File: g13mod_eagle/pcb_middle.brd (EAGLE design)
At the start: 134.2 x 33.2 mm, 0 parts

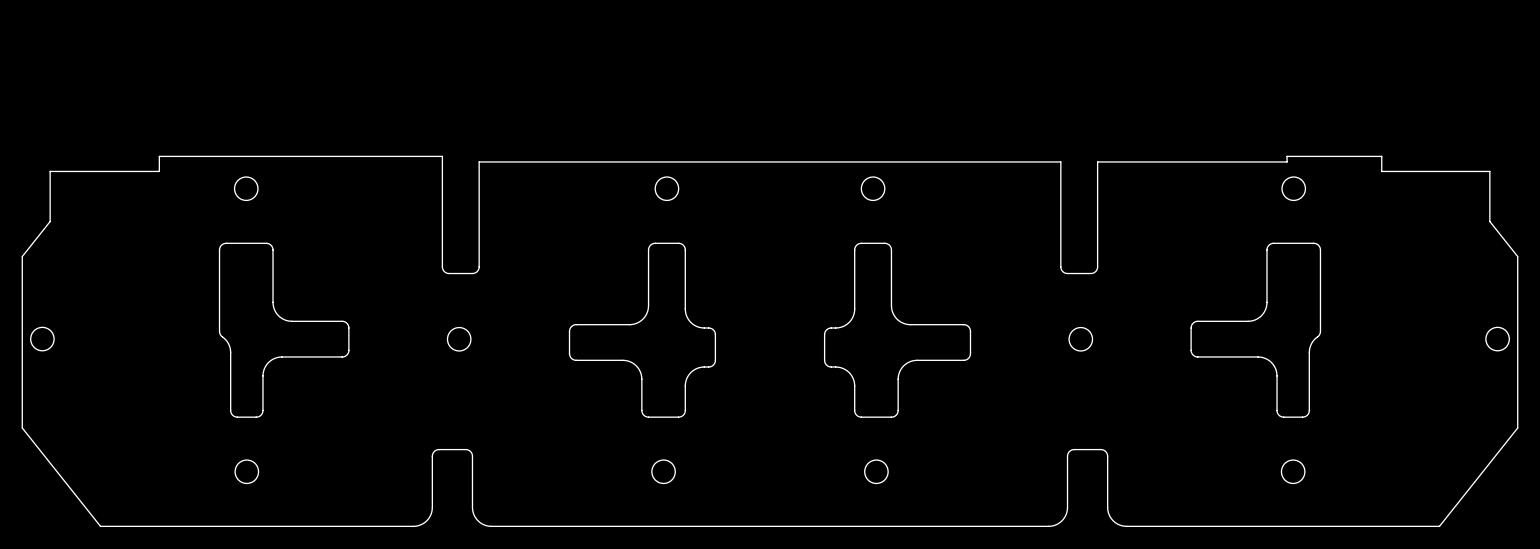
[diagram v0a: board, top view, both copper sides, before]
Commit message: Add switches
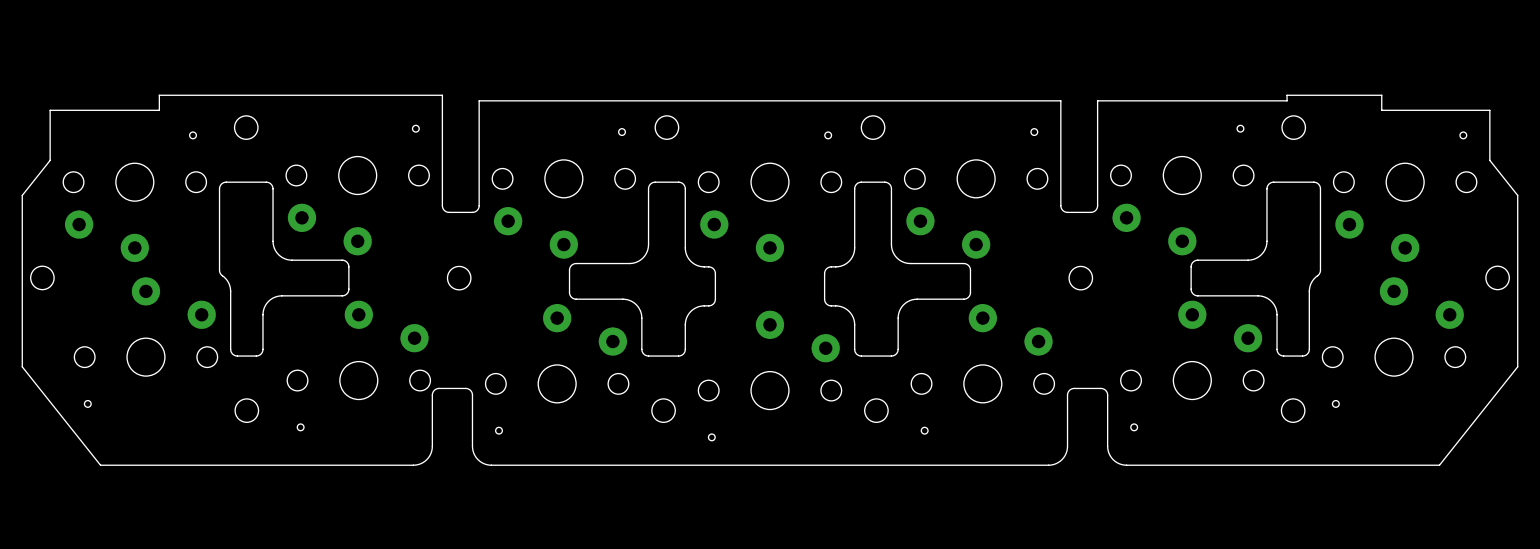
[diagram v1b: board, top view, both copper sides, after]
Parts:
- added U$1, U$10, U$11, U$12, U$13, U$14, U$2, U$3, U$4, U$5, U$6, U$7, U$8, U$9: KEYSWITCH-PLAIN-CHOC-1U, Keyboard:CHOC-1U
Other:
- outline, holes or cut-outs redrawn

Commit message: wiring middle pcb
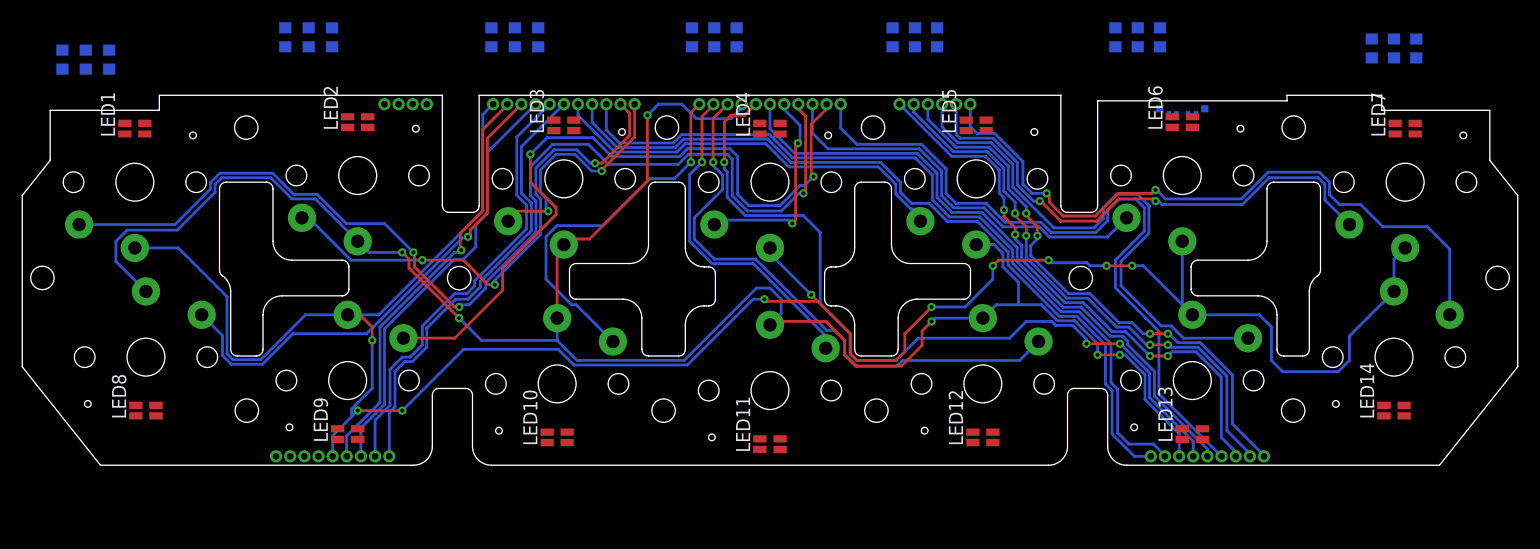
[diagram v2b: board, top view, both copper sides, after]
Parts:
- removed U$9: KEYSWITCH-PLAIN-CHOC-1U, Keyboard:CHOC-1U
- added D1: QLS6B-FKW-CNSNSF043, QLS6B-FKW-CNSNSF043:LED_QLS6B-FKW-CNSNSF043
- added G9: KEYSWITCH-PLAIN-CHOC-1U, Keyboard:CHOC-1U
- added JP1: (no value), pinhead-half-pitch:THROUHOLE04
- added JP2, JP3: (no value), pinhead-half-pitch:THROUHOLE11
- added JP4: (no value), pinhead-half-pitch:THROUHOLE06
- added JP8, JP9: (no value), pinhead-half-pitch:THROUHOLE09
- added LED1, LED10, LED11, LED12, LED13, LED14, LED2, LED3, LED4, LED5, LED6, LED7, LED8, LED9: B38G3RGB, led_rgb:B38G3RGB
- added R1, R10, R11, R12, R13, R14, R15, R16, R17, R18, R19, R2, R20, R21, R3, R4, R5, R6, R7, R8, R9: (no value), rcl:R0603
- renumbered U$1 to G1, U$10 to G10, U$11 to G11, U$12 to G12, U$13 to G13, U$14 to G14, U$2 to G2, U$3 to G6, U$4 to G3, U$5 to G5, U$6 to G4, U$7 to G7, U$8 to G8
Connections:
- new net B: JP1.4, JP8.9, R11.1, R14.1, R17.1, R2.1, R20.1, R5.1, R8.1
- new net CN6_10: G5.CHOC2, JP2.5
- new net CN6_11: JP2.6, JP8.1
- new net CN6_13: JP2.7, JP8.2
- new net CN6_14: JP2.8, JP8.3
- new net CN6_16: G8.CHOC2, JP2.9
- new net CN6_17: JP2.10, JP8.4
- new net CN6_18: G1.CHOC1, G13.CHOC1, G14.CHOC1, G4.CHOC1, G6.CHOC1, G7.CHOC1, G9.CHOC1, JP2.11, JP8.5
- new net CN6_3: G12.CHOC2, JP3.9
- new net CN6_4: G11.CHOC2, JP3.10
- new net CN6_5: G10.CHOC2, JP3.11
- new net CN6_6: G3.CHOC2, JP2.1
- new net CN6_7: G2.CHOC2, JP2.2
- new net CN6_8: JP2.3, JP9.8
- new net CN6_9: JP2.4, JP9.9
- new net CN7_1: G14.CHOC2, JP4.1
- new net CN7_10: G6.CHOC2, JP3.3
- new net CN7_11: G1.CHOC2, JP3.4
- new net CN7_12: G4.CHOC2, JP3.5
- new net CN7_13: JP3.6, JP9.5
- new net CN7_14: JP3.7, JP9.6
- new net CN7_15: G10.CHOC1, G11.CHOC1, G12.CHOC1, G2.CHOC1, G3.CHOC1, G5.CHOC1, G8.CHOC1, JP3.8, JP9.7
- new net CN7_2: G7.CHOC2, JP4.2
- new net CN7_3: G13.CHOC2, JP4.3
- new net CN7_4: JP4.4, JP9.1
- new net CN7_6: JP4.5, JP9.2
- new net CN7_7: JP4.6, JP9.3
- new net CN7_8: JP3.1, JP9.4
- new net CN7_9: G9.CHOC2, JP3.2
- new net G: JP1.2, JP8.7, R1.1, R10.1, R13.1, R16.1, R19.1, R4.1, R7.1
- new net N$1: LED1.1, R1.2
- new net N$10: LED4.1, R10.2
- new net N$11: LED4.2, R11.2
- new net N$12: LED4.4, R12.2
- new net N$13: LED5.1, R13.2
- new net N$14: LED5.2, R14.2
- new net N$15: LED5.4, R15.2
- new net N$16: LED6.1, R16.2
- new net N$17: LED6.2, R17.2
- new net N$18: LED6.4, R18.2
- new net N$19: LED7.1, R19.2
- new net N$2: LED1.2, R2.2
- new net N$20: LED7.2, R20.2
- new net N$21: LED7.4, R21.2
- new net N$3: LED1.4, R3.2
- new net N$4: LED2.1, R4.2
- new net N$5: LED2.2, R5.2
- new net N$6: LED2.4, R6.2
- new net N$7: LED3.1, R7.2
- new net N$8: LED3.2, R8.2
- new net N$9: LED3.4, R9.2
- new net R: JP1.3, JP8.8, R12.1, R15.1, R18.1, R21.1, R3.1, R6.1, R9.1
- new net V: D1.1, D1.3, D1.5, JP1.1, JP8.6, LED1.3, LED10.3, LED11.3, LED12.3, LED13.3, LED14.3, LED2.3, LED3.3, LED4.3, LED5.3, LED6.3, LED7.3, LED8.3, LED9.3
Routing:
- net CN6_18: track 0.00 -> 206.6 mm, vias 0 -> 10
- net CN7_15: track 0.00 -> 175.7 mm, vias 0 -> 6
- net CN7_11: track 0.00 -> 97.6 mm, vias 0 -> 3
- net CN7_14: track 0.00 -> 71.9 mm, vias 0 -> 3
- net CN6_8: track 0.00 -> 71.6 mm
- net CN6_9: track 0.00 -> 70.4 mm
- net CN7_9: track 0.00 -> 65.2 mm, vias 0 -> 2
- net CN7_8: track 0.00 -> 64.0 mm
- net CN7_1: track 0.00 -> 61.6 mm, vias 0 -> 2
- net CN7_13: track 0.00 -> 57.5 mm
- net CN6_3: track 0.00 -> 51.3 mm, vias 0 -> 1
- net CN7_4: track 0.00 -> 50.7 mm, vias 0 -> 4
- net CN7_7: track 0.00 -> 50.5 mm, vias 0 -> 4
- net CN7_6: track 0.00 -> 50.2 mm, vias 0 -> 4
- net CN7_3: track 0.00 -> 49.5 mm
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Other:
- outline, holes or cut-outs redrawn

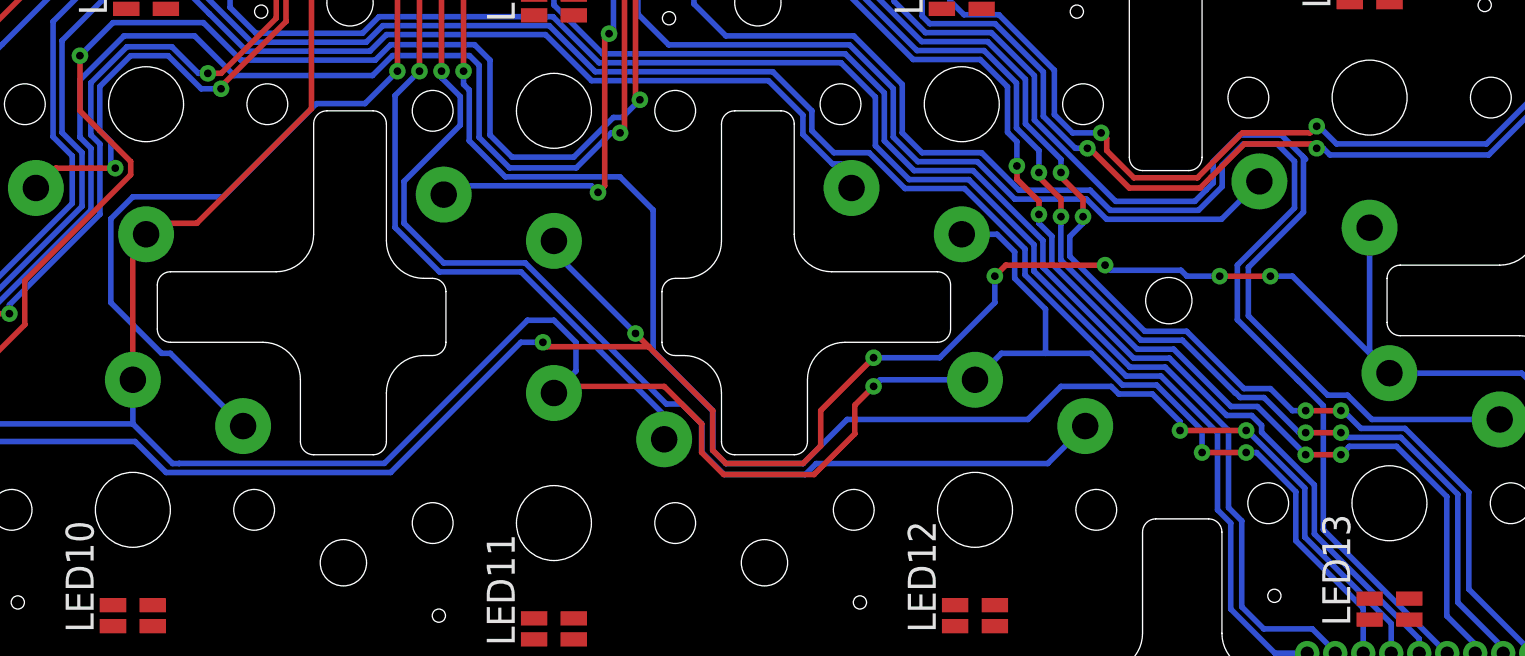
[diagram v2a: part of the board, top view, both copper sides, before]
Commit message: wiring middle pcb
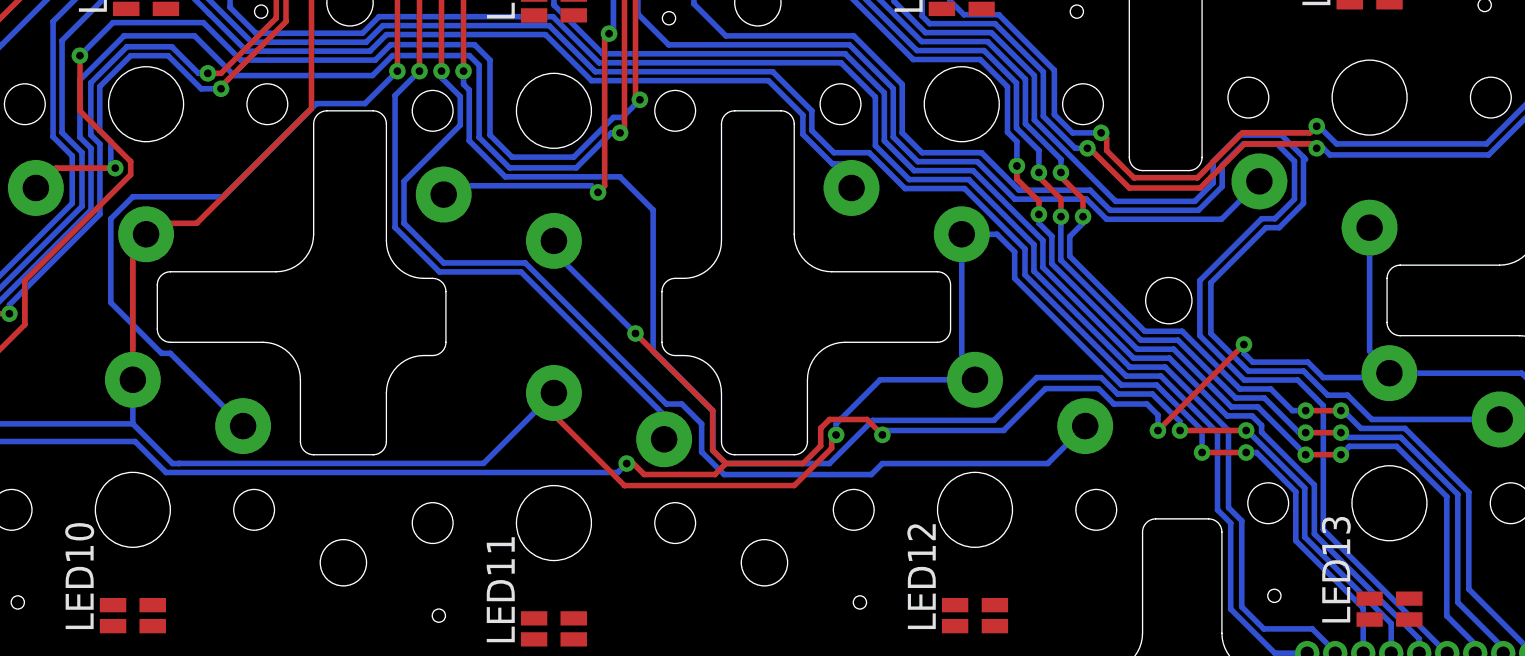
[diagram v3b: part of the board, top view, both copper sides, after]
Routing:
- net CN7_15: track 175.7 -> 171.3 mm
- net CN7_3: track 49.5 -> 52.7 mm
- net CN7_8: track 64.0 -> 67.2 mm
- net CN6_18: track 206.6 -> 206.9 mm, vias 10 -> 8

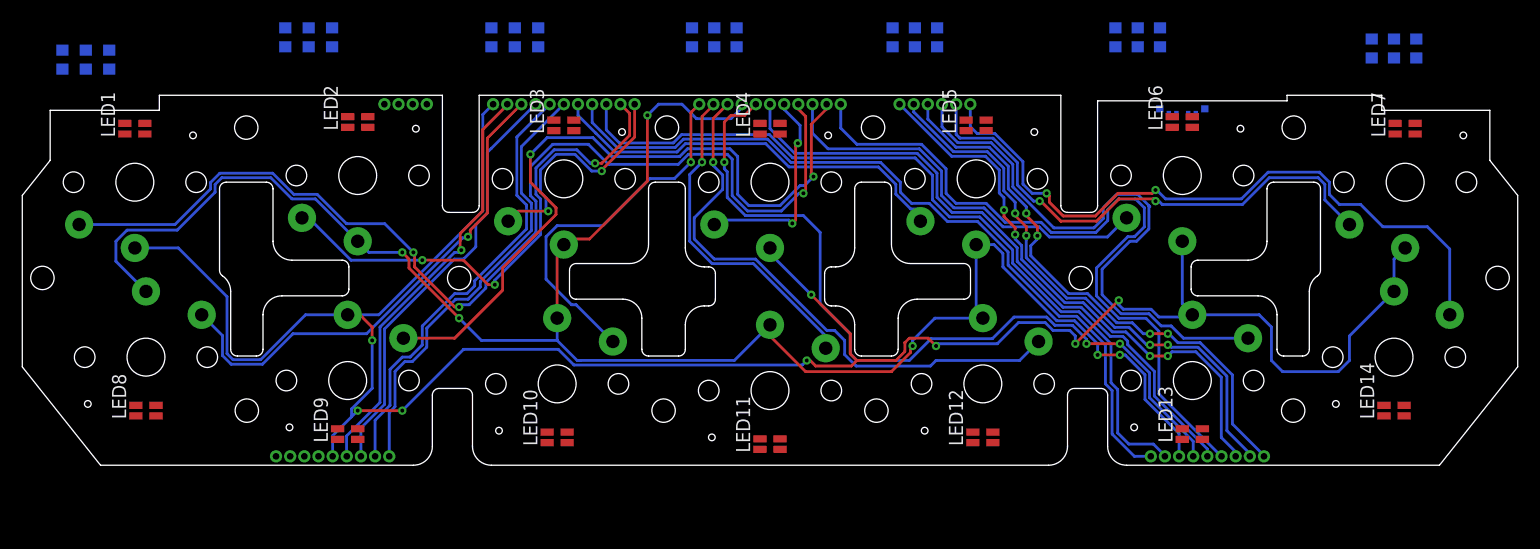
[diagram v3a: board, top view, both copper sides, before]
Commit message: wiring middle pcb
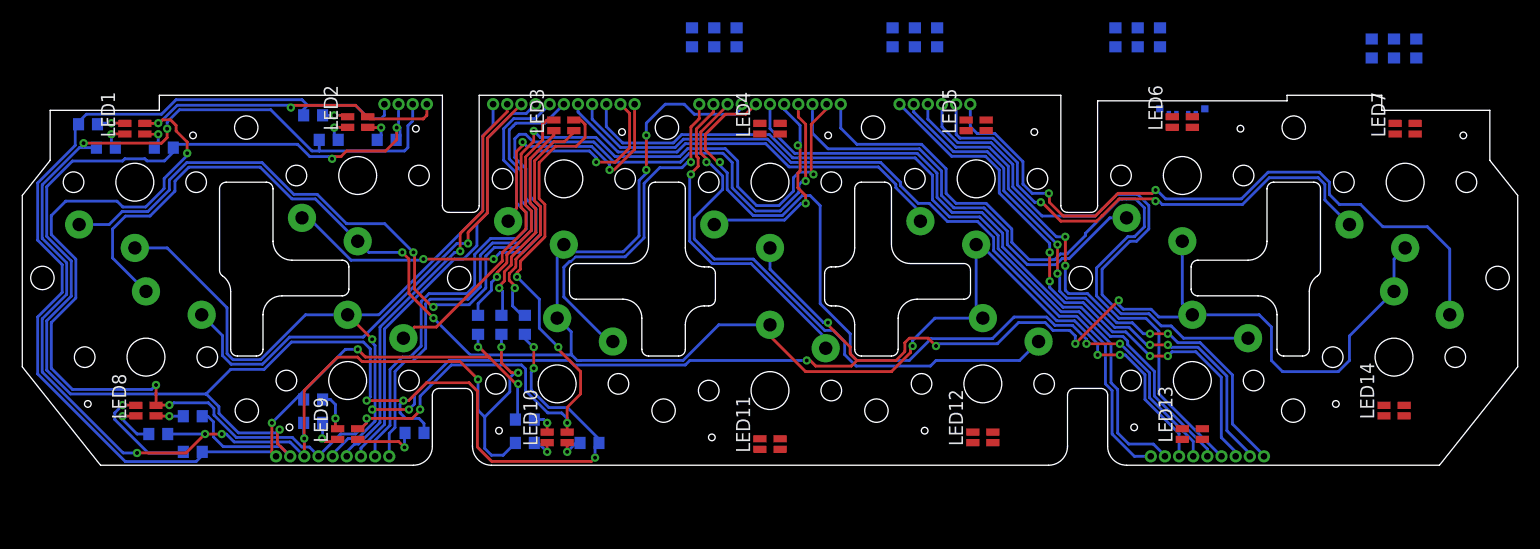
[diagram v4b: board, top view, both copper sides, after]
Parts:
- added R22, R23, R24, R25, R26, R27, R28, R29, R30: (no value), rcl:R0603
- moved R8 26.4 mm to (-26.2, -12.8)
- moved R9 26.0 mm to (-22.0, -12.8)
- moved R7 25.8 mm to (-24.1, -12.8)
- moved R6 12.9 mm to (-34.4, 3.80), turned to 0 degrees
- moved R3 12.1 mm to (-54.4, 3.10), turned to 0 degrees
- moved R4 9.37 mm to (-39.6, 3.80), turned to 180 degrees
- moved R1 8.10 mm to (-59.6, 3.10), turned to 180 degrees
- moved R5 7.20 mm to (-41.0, 6.00), turned to 180 degrees
- moved R2 6.10 mm to (-61.2, 5.20), turned to 180 degrees
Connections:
- new net N$22: LED8.1, R22.2
- new net N$23: LED8.2, R23.2
- new net N$24: LED8.4, R24.2
- new net N$25: LED9.1, R25.2
- new net N$26: LED9.2, R26.2
- new net N$27: LED9.4, R27.2
- new net N$28: LED10.1, R28.2
- new net N$29: LED10.2, R29.2
- new net N$30: LED10.4, R30.2
- net B: now also R23.1, R26.1, R29.1
- net G: now also R22.1, R25.1, R28.1
- net R: now also R24.1, R27.1, R30.1
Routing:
- net R: track 0.00 -> 163.5 mm, vias 0 -> 8
- net V: track 0.00 -> 160.3 mm, vias 0 -> 10
- net G: track 0.00 -> 139.8 mm, vias 0 -> 9
- net B: track 0.00 -> 118.7 mm, vias 0 -> 4
- net N$8: track 0.00 -> 21.1 mm, vias 0 -> 1
- net N$9: track 0.00 -> 21.0 mm, vias 0 -> 1
- net N$7: track 0.00 -> 19.2 mm, vias 0 -> 1
- net N$23: track 0.00 -> 10.2 mm, vias 0 -> 1
- net CN7_11: track 97.6 -> 104.5 mm
- net CN7_15: track 171.3 -> 178.1 mm, vias 6 -> 7
- net N$27: track 0.00 -> 6.17 mm, vias 0 -> 1
- net CN6_11: track 39.9 -> 45.1 mm
- net CN6_13: track 39.9 -> 44.7 mm
- net N$22: track 0.00 -> 4.40 mm, vias 0 -> 1
- net CN7_14: track 72.2 -> 76.5 mm
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
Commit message: wiring middle pcb
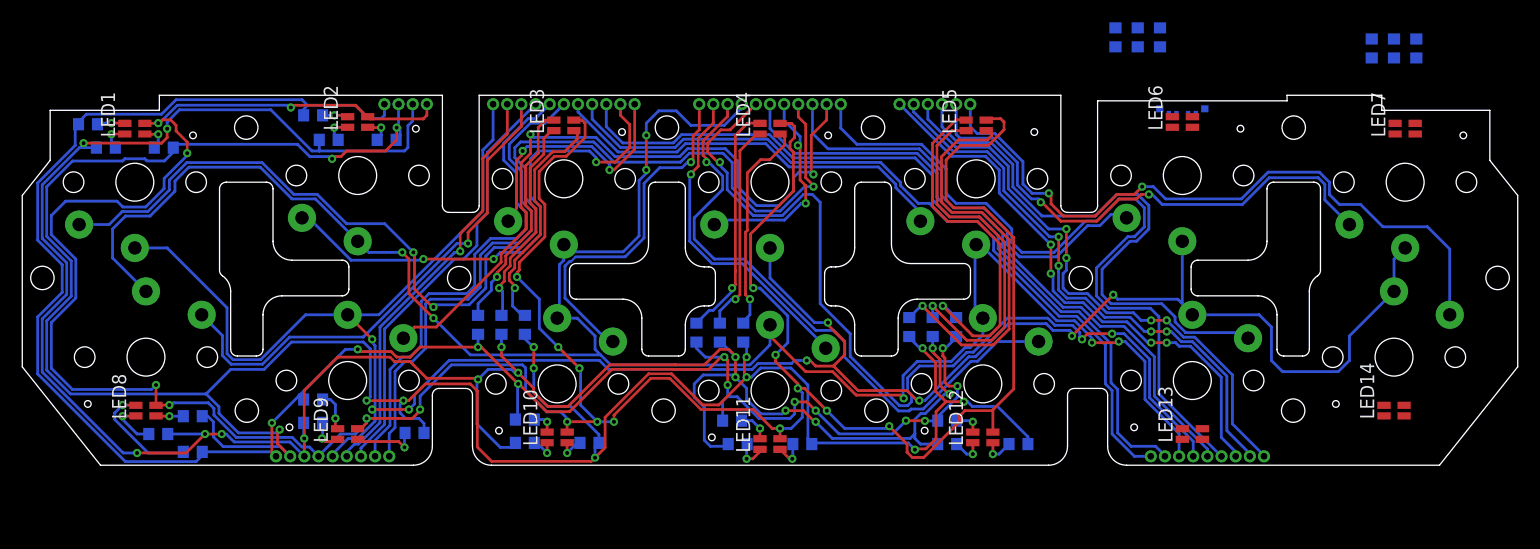
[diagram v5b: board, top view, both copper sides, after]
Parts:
- added R31, R32, R33, R34, R35, R36: (no value), rcl:R0603
- moved R12 26.9 mm to (-2.40, -13.5)
- moved R11 26.7 mm to (-6.60, -13.5)
- moved R10 26.5 mm to (-4.50, -13.5)
- moved R14 26.1 mm to (16.7, -13.0)
- moved R13 26.0 mm to (14.6, -13.0)
- moved R15 26.0 mm to (12.5, -13.0)
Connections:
- new net N$31: LED11.1, R31.2
- new net N$32: LED11.2, R32.2
- new net N$33: LED11.4, R33.2
- new net N$34: LED12.1, R34.2
- new net N$35: LED12.2, R35.2
- new net N$36: LED12.4, R36.2
- net B: now also R32.1, R35.1
- net G: now also R31.1, R34.1
- net R: now also R33.1, R36.1
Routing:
- net V: track 160.3 -> 279.6 mm, vias 10 -> 19
- net G: track 139.8 -> 209.2 mm, vias 9 -> 15
- net R: track 163.5 -> 231.6 mm, vias 8 -> 13
- net B: track 118.7 -> 181.8 mm, vias 4 -> 12
- net N$15: track 0.00 -> 37.0 mm, vias 0 -> 1
- net N$13: track 0.00 -> 32.8 mm, vias 0 -> 1
- net N$14: track 0.00 -> 32.6 mm, vias 0 -> 1
- net N$11: track 0.00 -> 21.2 mm, vias 0 -> 1
- net N$12: track 0.00 -> 19.7 mm, vias 0 -> 1
- net N$10: track 0.00 -> 18.8 mm, vias 0 -> 1
- net CN7_15: track 178.1 -> 186.9 mm
- net CN7_14: track 76.5 -> 82.3 mm
- net CN6_3: track 52.3 -> 55.6 mm
- net N$31: track 0.00 -> 3.01 mm, vias 0 -> 1
- net N$32: track 0.00 -> 2.86 mm, vias 0 -> 1
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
